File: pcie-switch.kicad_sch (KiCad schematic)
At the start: 82 parts, among them Q2 BSS138PW,115, Q3 BSS138PW,115, U1 PI7C9X3G606GP, U3 MAX3373EEKA+, U6 NVT4858_XQFN

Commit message: [#100765] Update schematic
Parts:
- added C31, C58: C_220n_0402, antmicro-footprints:C_0402_1005Metric, symbol antmicroCapacitors0402:C_220n_0402
- added R44, R45, R46, R49, R50, R68: R_5k1_0402, antmicro-footprints:R_0402_1005Metric, symbol antmicroResistors0402:R_5k1_0402
- added R47, R48, R51: R_330R_0402, antmicro-footprints:R_0402_1005Metric, symbol antmicroResistors0402:R_330R_0402
- added R65, R67: R_0R_0402, antmicro-footprints:R_0402_1005Metric, symbol antmicroResistors0402:R_0R_0402
- added TP1, TP25, TP3, TP31: TP_0.75mm_SMD, antmicro-footprints:TP_SMD_0.75mm, symbol antmicroTestPoints:TP_0.75mm_SMD
- added TP16, TP17: TP_1mm_SMD, antmicro-footprints:TP_SMD_1mm, symbol antmicroTestPoints:TP_1mm_SMD
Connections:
- net +1V8: now also R44.2, R45.2, R46.2, R49.1, R50.1, R68.2
- net C_MODE0: now also R46.1, R48.2
- net C_MODE1: now also R45.1, R47.2
- net GND: now also Q2.2 (S), Q3.2 (S), R47.1, R48.1, R51.2; no longer R21.1, R38.1
- net MISO: no longer U1.M11 (~{EECS})
- net PCIe_{x2_1}.RX0_N: no longer U1.M10 (PER5_N)
- net PCIe_{x2_1}.RX0_P: no longer U1.M9 (PER5_P)
- net PCIe_{x2_1}.TX0_N: no longer C22.2
- net PCIe_{x2_1}.TX0_P: no longer C21.2
- net PCIe_{x2}.~{RST}: now also TP31.1
- net at U1.A1 (REFCLKO1_N): now also TP25.1
- net at U1.A2 (REFCLKO1_P): now also TP3.1
- net at U1.A7 (PER1_N): now also R67.2
- net at U1.A8 (PER1_P): now also R65.2
- net at U1.C7 (PET1_N): now also C58.2
- net at U1.C8 (PET1_P): now also C31.2
- net ~{CLKREQ1}: now reaches U1.E4 (~{CLKREQ1})
- net ~{CLKREQ1}: now also R68.1, TP1.1
- net at R35.1, U1.M1 (SHDA_I2C): now also TP17.1
- net at D1.1 (C): now also R21.2; no longer Q2.3 (D)
- net ~{PM_L11_EN}: now reaches U1.E1 (~{PM_L11_EN})
- net ~{PM_L11_EN}: now also R50.2, R51.1
- net at U1.E9 (~{HOT_PLUG_EN}): now also R49.2
- net at R34.1, U1.L1 (SHCL_I2C): now also TP16.1
- net at U1.M2 (~{SHPCINT}): now also R44.1
- net at D2.1 (C): now also R38.2; no longer Q3.3 (D)
- net JTAG_TCK renamed TCK
- net JTAG_TDI renamed TDI
- net JTAG_TDO renamed TDO
- net JTAG_TMS renamed TMS
- net JTAG_~{RESET} renamed ~{RESET}
- new net: Q2.3 (D), R21.1
- new net: Q3.3 (D), R38.1
- new net CS: U1.M11 (~{EECS})
- new net PCIe_{x2_1}.RX1_N: U1.M10 (PER5_N)
- new net PCIe_{x2_1}.RX1_P: U1.M9 (PER5_P)
- new net PCIe_{x2_1}.TX1_N: C22.2
- new net PCIe_{x2_1}.TX1_P: C21.2
- new net PCIe_{x2}.RX1_N: C58.1
- new net PCIe_{x2}.RX1_P: C31.1
- new net PCIe_{x2}.TX1_N: R67.1
- new net PCIe_{x2}.TX1_P: R65.1
- no-connect marks 27 -> 19
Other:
- note added: "Chip Mode bootstrap"
- note added: "Details: p.28 in the datasheet"
- note added: "HP disabled"
- note added: "Hot Plug LEDs"
- note added: "JTAG"
- note added: "SPI EEPROM & I2C"
- moved on the sheet: C15, C16, C17, C35, C36, C40, C42, C44, C45, C5, C6, D1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

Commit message: [#100765] Change sheet format to A3, update schematic
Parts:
- removed D3, D4, D5: LED_G_0603_LG_L29K-G2J1-24-Z, antmicro-footprints:LED_0603_1608Metric_G, symbol antmicroLEDIndicationDiscrete:LED_G_0603_LG_L29K-G2J1-24-Z
- removed R39, R41: R_470R_0402, antmicro-footprints:R_0402_1005Metric, symbol antmicroResistors0402:R_470R_0402
- removed U6: NVT4858_XQFN, antmicro-footprints:SOT1161-2, symbol antmicroLogicTranslatorsLevelShifters:NVT4858_XQFN
- added D10, D8, D9: LED_G_0603_LG_L29K-G2J1-24-Z, antmicro-footprints:LED_0603_1608Metric_G, symbol antmicroLEDIndicationDiscrete:LED_G_0603_LG_L29K-G2J1-24-Z
- added Q7, Q8, Q9: BSS138PW,115, antmicro-footprints:SC70-3, symbol antmicroTransistorsFETsMOSFETsSingle:BSS138PW,115
- added R18, R82: R_470R_0402, antmicro-footprints:R_0402_1005Metric, symbol antmicroResistors0402:R_470R_0402
- added R19, R39, R41: R_10k_0402, antmicro-footprints:R_0402_1005Metric, symbol antmicroResistors0402:R_10k_0402
- added TP32: TP_1mm_SMD, antmicro-footprints:TP_SMD_1mm, symbol antmicroTestPoints:TP_1mm_SMD
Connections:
- net +1V8: now also R19.2, R39.2, R41.2
- net +3V3: now also Q7.3 (D), Q8.3 (D), Q9.3 (D)
- net GND: now also R40.2, R18.2, R82.2
- net at U1.E10 (~{PORTGOOD1}): now also TP32.1
- net at R40.1: now also D9.1 (C)
- net ~{PGOOD0} renamed ~{PORTGOOD0}
- net ~{PORTGOOD0}: now also Q7.1 (G), R19.1
- net ~{PGOOD4} renamed ~{PORTGOOD4}
- net ~{PORTGOOD4}: now also Q8.1 (G), R39.1
- net ~{PGOOD5} renamed ~{PORTGOOD5}
- net ~{PORTGOOD5}: now also Q9.1 (G), R41.1
- new net: D9.2 (A), Q8.2 (S)
- new net: D10.2 (A), Q9.2 (S)
- new net: D10.1 (C), R82.1
- new net: D8.1 (C), R18.1
- new net: D8.2 (A), Q7.2 (S)
- no-connect marks 19 -> 11
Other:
- note added: "PCIe Switch"
- note added: "Status LEDs"
- company: (none) -> Antmicro
- title: (none) -> antmicro-jetson-orin-baseboard-pcie-switch-expansion-hw
- moved on the sheet: C10, C11, C12, C13, C14, C15, C16, C17, C18, C2, C20, C21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

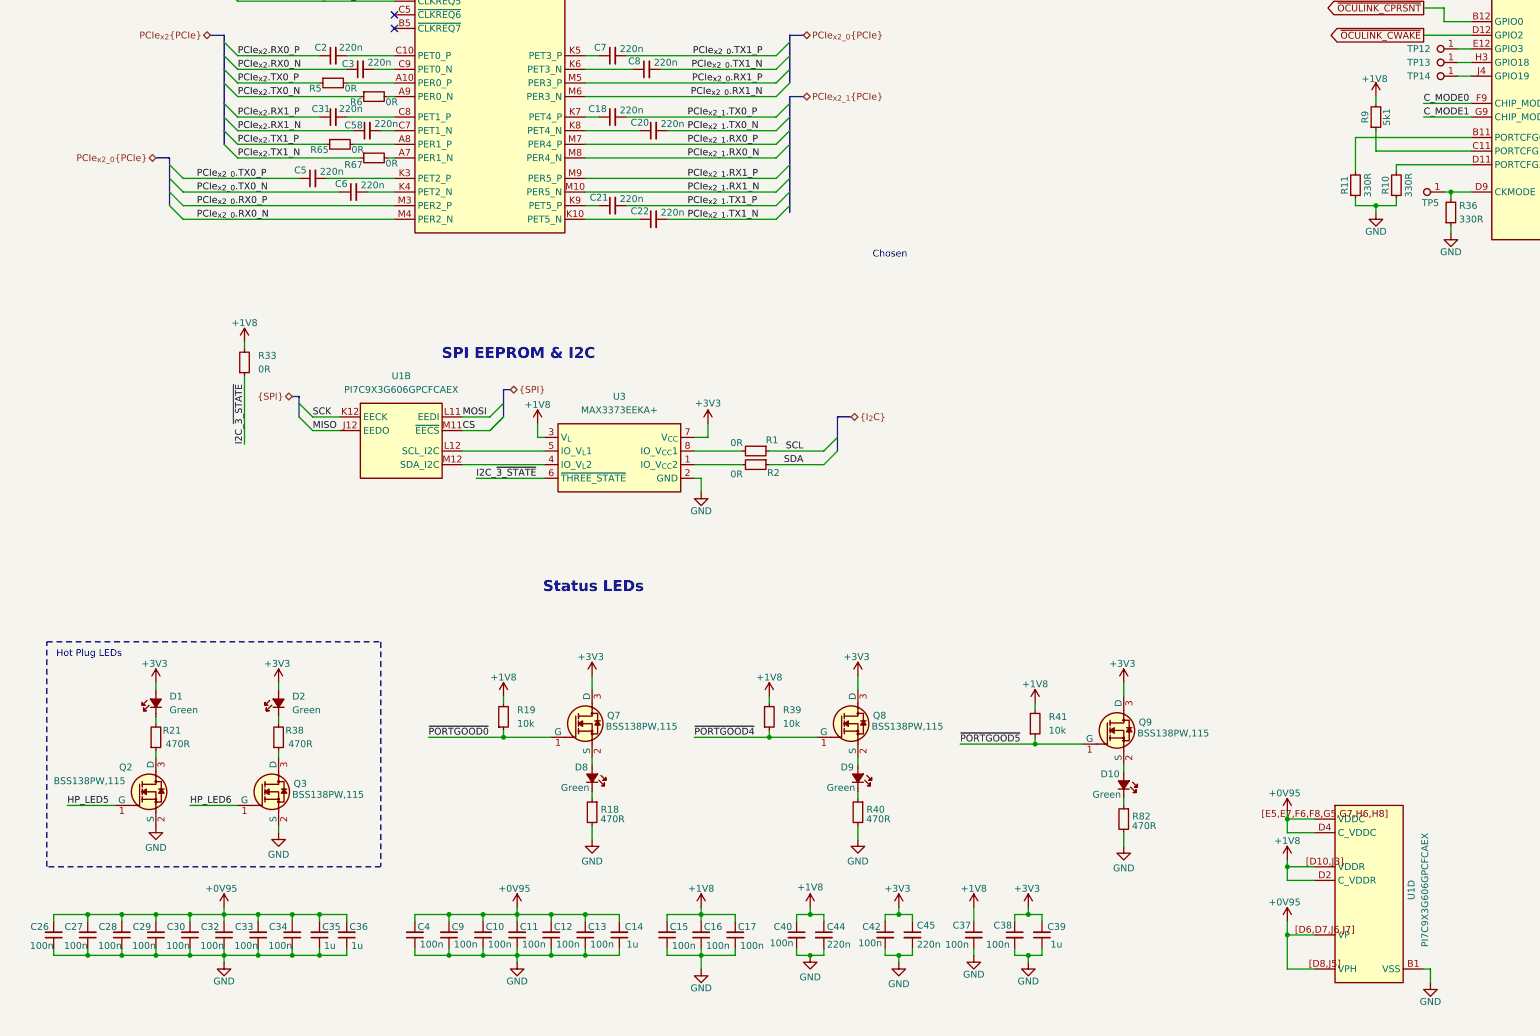
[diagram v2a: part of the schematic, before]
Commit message: [#100765] Prettify decoupling caps
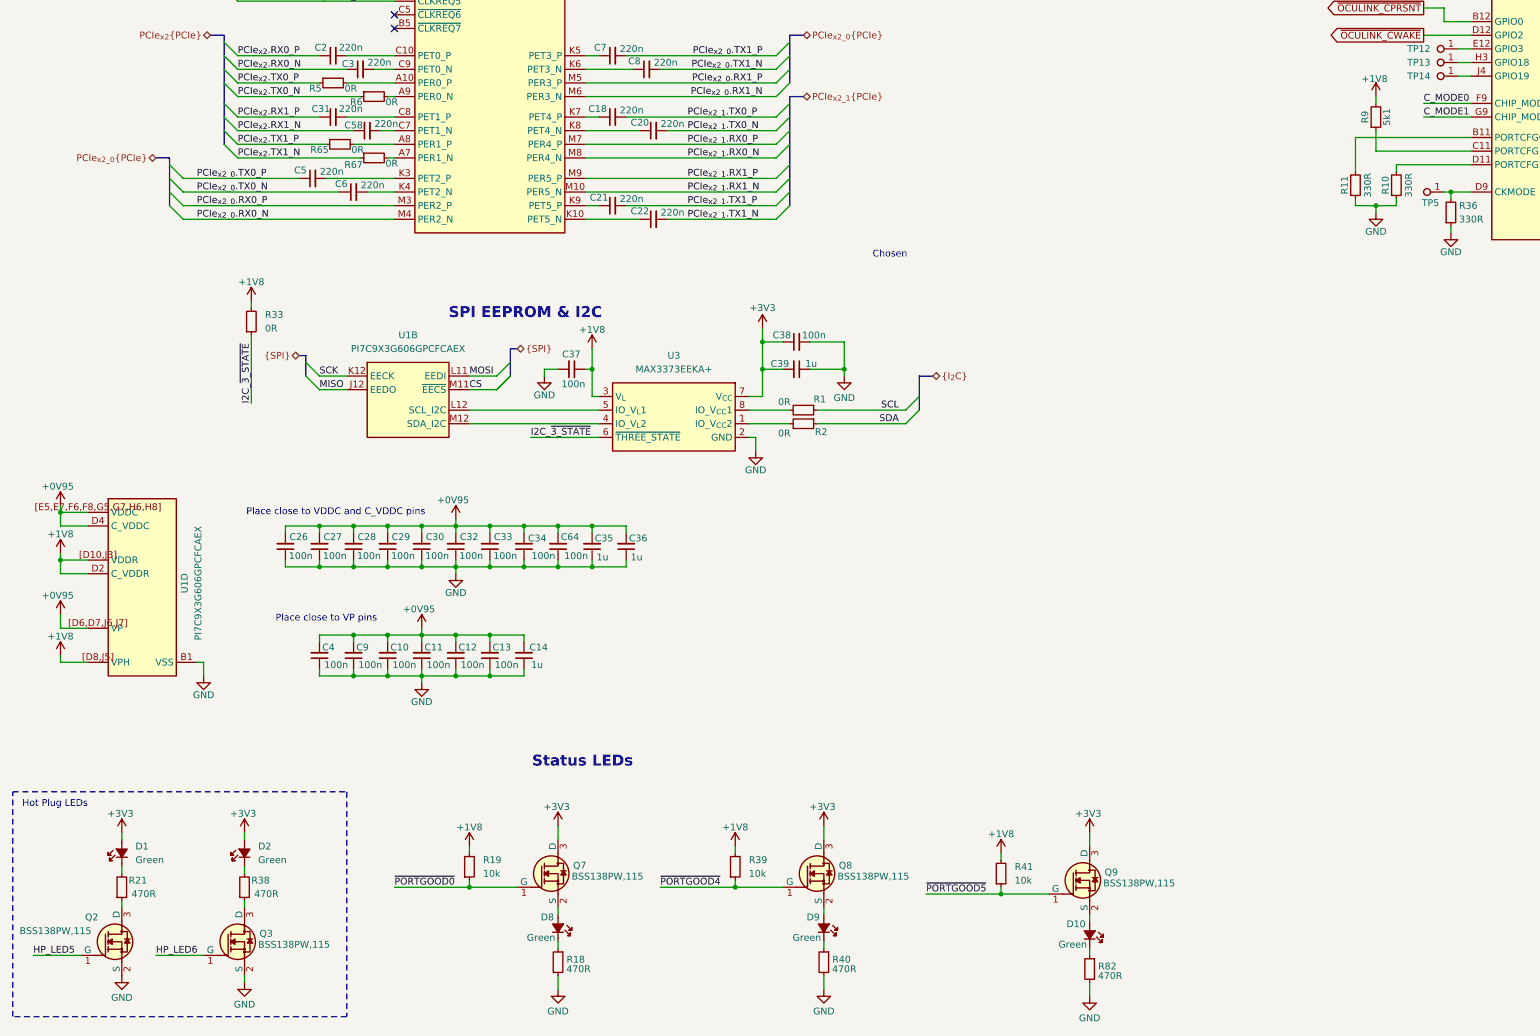
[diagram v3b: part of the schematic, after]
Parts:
- removed C15, C16, C17: C_100n_0402, antmicro-footprints:C_0402_1005Metric, symbol antmicroCapacitors0402:C_100n_0402
- removed C40, C42: C_100n_16V_X7R_0402, antmicro-footprints:C_0402_1005Metric, symbol antmicroCapacitors0402:C_100n_16V_X7R_0402
- removed C44, C45: C_220n_0402, antmicro-footprints:C_0402_1005Metric, symbol antmicroCapacitors0402:C_220n_0402
- added C64: C_100n_0402, antmicro-footprints:C_0402_1005Metric, symbol antmicroCapacitors0402:C_100n_0402
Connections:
- net +0V95: now also C64.2; no longer U1.[D8,J5] (VPH)
- net +1V8: now also U1.[D8,J5] (VPH)
- net GND: now also C64.1
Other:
- note added: "Place close to VDDC and C_VDDC pins"
- note added: "Place close to VP pins"
- moved on the sheet: C10, C11, C12, C13, C14, C26, C27, C28, C29, C30, C32, C33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

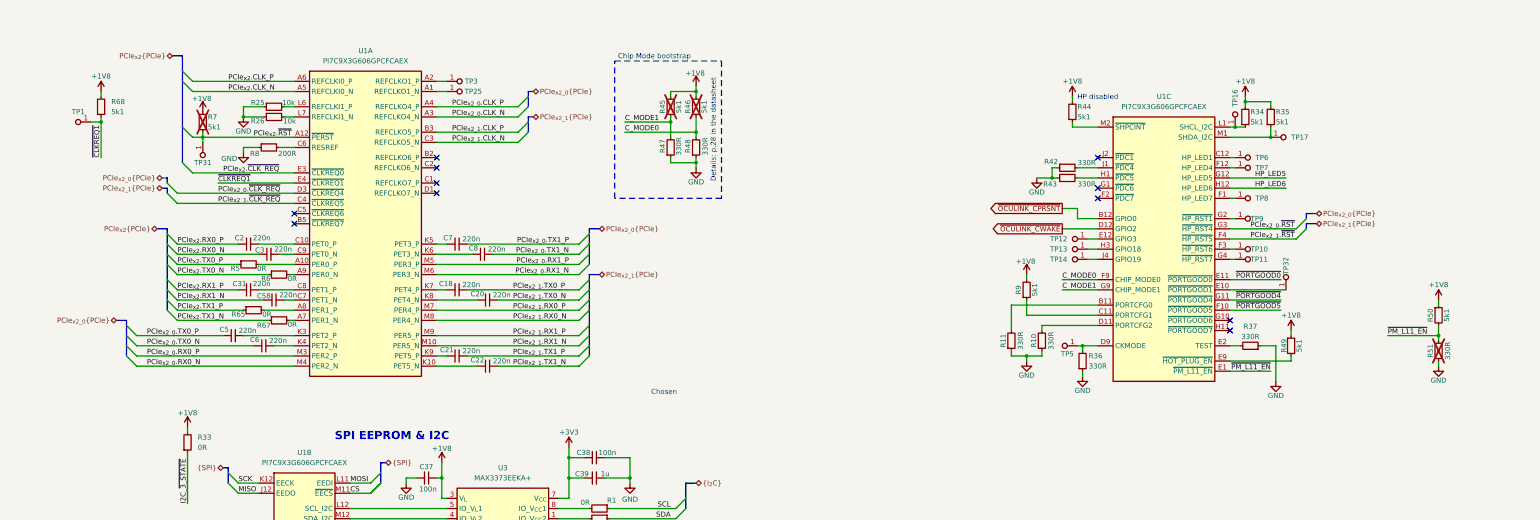
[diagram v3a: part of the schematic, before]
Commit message: [#100765] WIP: Apply review changes
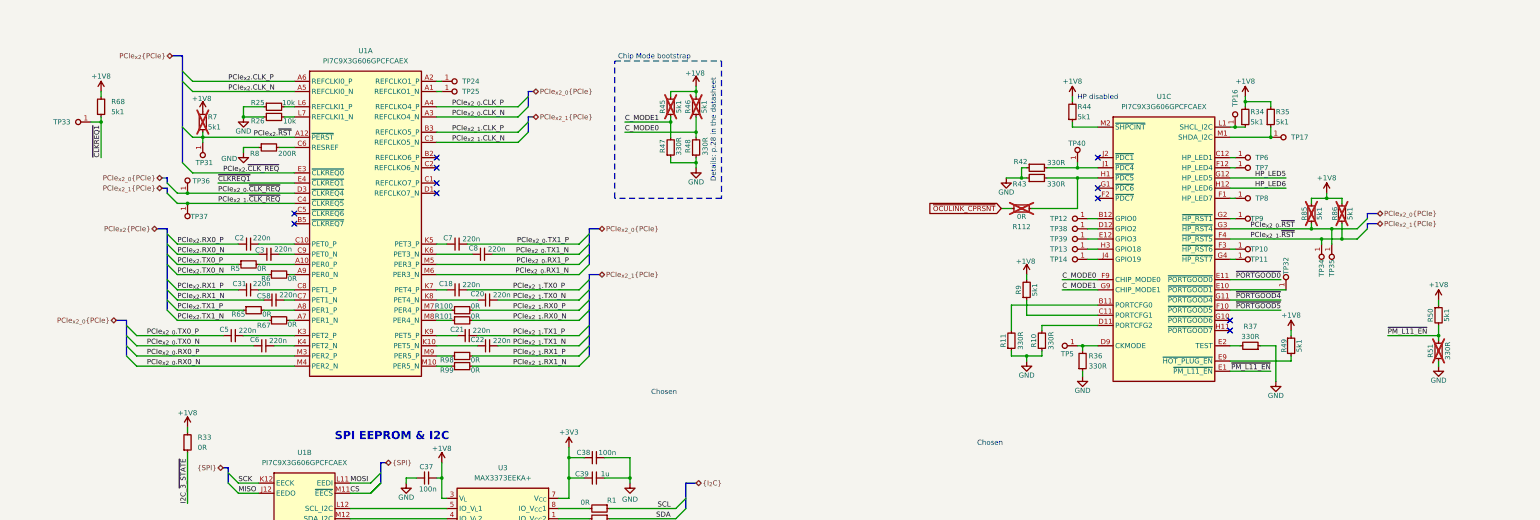
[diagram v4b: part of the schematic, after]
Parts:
- removed TP1, TP25, TP3, TP31: TP_0.75mm_SMD, antmicro-footprints:TP_SMD_0.75mm, symbol antmicroTestPoints:TP_0.75mm_SMD
- added R100, R101, R112, R98, R99: R_0R_0402, antmicro-footprints:R_0402_1005Metric, symbol antmicroResistors0402:R_0R_0402
- added R85, R86: R_5k1_0402, antmicro-footprints:R_0402_1005Metric, symbol antmicroResistors0402:R_5k1_0402
- added TP24, TP25, TP31, TP33, TP34, TP35, TP36, TP37, TP38, TP39, TP40: TP_1mm_SMD, antmicro-footprints:TP_SMD_1mm, symbol antmicroTestPoints:TP_1mm_SMD
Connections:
- net +1V8: now also R85.1, R86.1
- net PCIe_{x2_0}.~{CLK_REQ}: now also TP36.1
- net PCIe_{x2_0}.~{RST}: now also R85.2, TP35.1
- net PCIe_{x2_1}.RX0_N: now also R101.2; no longer U1.M8 (PER4_N)
- net PCIe_{x2_1}.RX0_P: now also R100.2; no longer U1.M7 (PER4_P)
- net PCIe_{x2_1}.RX1_N: now also R99.2; no longer U1.M10 (PER5_N)
- net PCIe_{x2_1}.RX1_P: now also R98.2; no longer U1.M9 (PER5_P)
- net PCIe_{x2_1}.~{CLK_REQ}: now also TP37.1
- net PCIe_{x2_1}.~{RST}: now also R86.2, TP34.1
- net PCIe_{x2}.~{RST}: now also TP31.1
- net ~{CLKREQ1}: now also TP33.1
- net ~{OCULINK_CPRSNT}: now also R112.1; no longer U1.B12 (GPIO0)
- net at U1.A2 (REFCLKO1_P): now also TP24.1
- net at U1.A1 (REFCLKO1_N): now also TP25.1
- net at U1.E12 (GPIO3): now also TP39.1; no longer TP12.1
- net at R43.2, U1.H1 (~{PDC5}): now also R112.2
- net at R42.2, U1.J1 (~{PDC4}): now also TP40.1
- net ~{OCULINK_CWAKE}: no longer names the net of U1.D12 (GPIO2)
- net ~{OCULINK_CWAKE}: now also TP38.1
- new net: R99.1, U1.M10 (PER5_N)
- new net: R100.1, U1.M7 (PER4_P)
- new net: R101.1, U1.M8 (PER4_N)
- new net: R98.1, U1.M9 (PER5_P)
- new net: TP12.1, U1.B12 (GPIO0)
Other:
- moved on the sheet: C21, C22, R42, R43, TP12

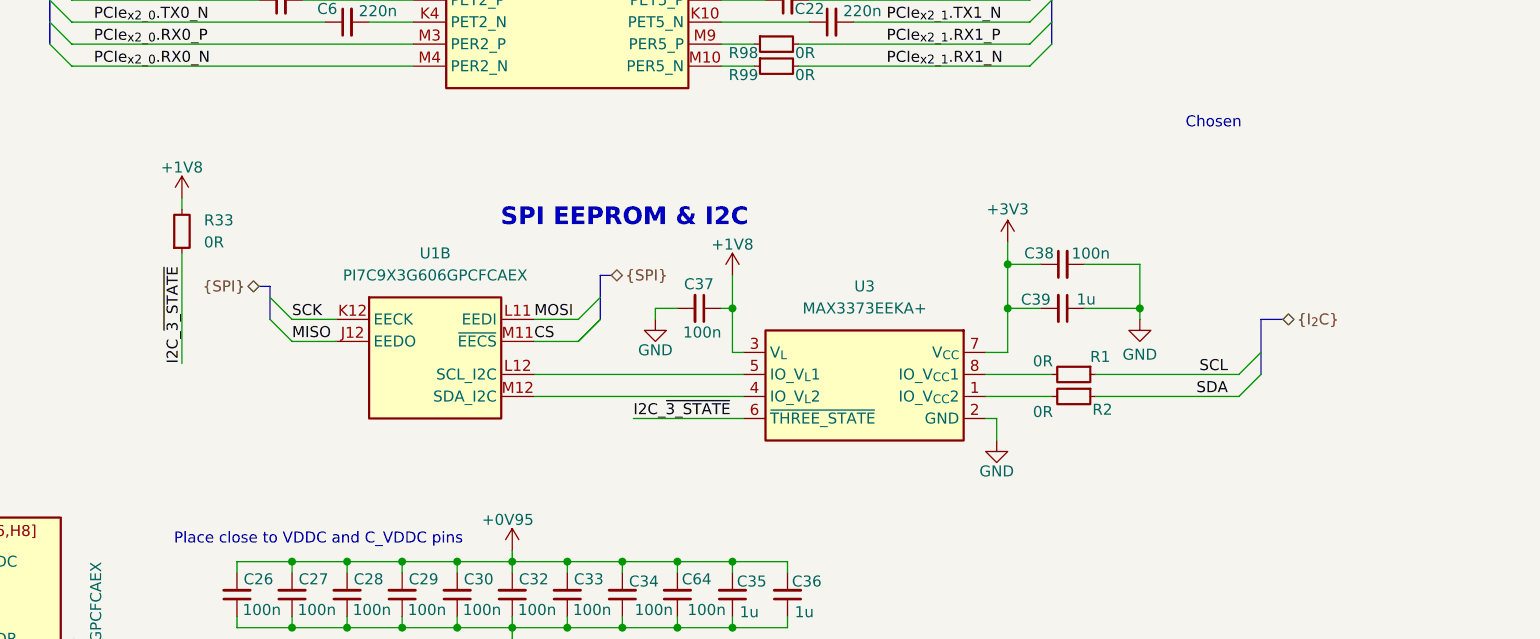
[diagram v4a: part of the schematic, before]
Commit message: [#100765] Change MAX3373EEKA+ to NTS0302JKZ
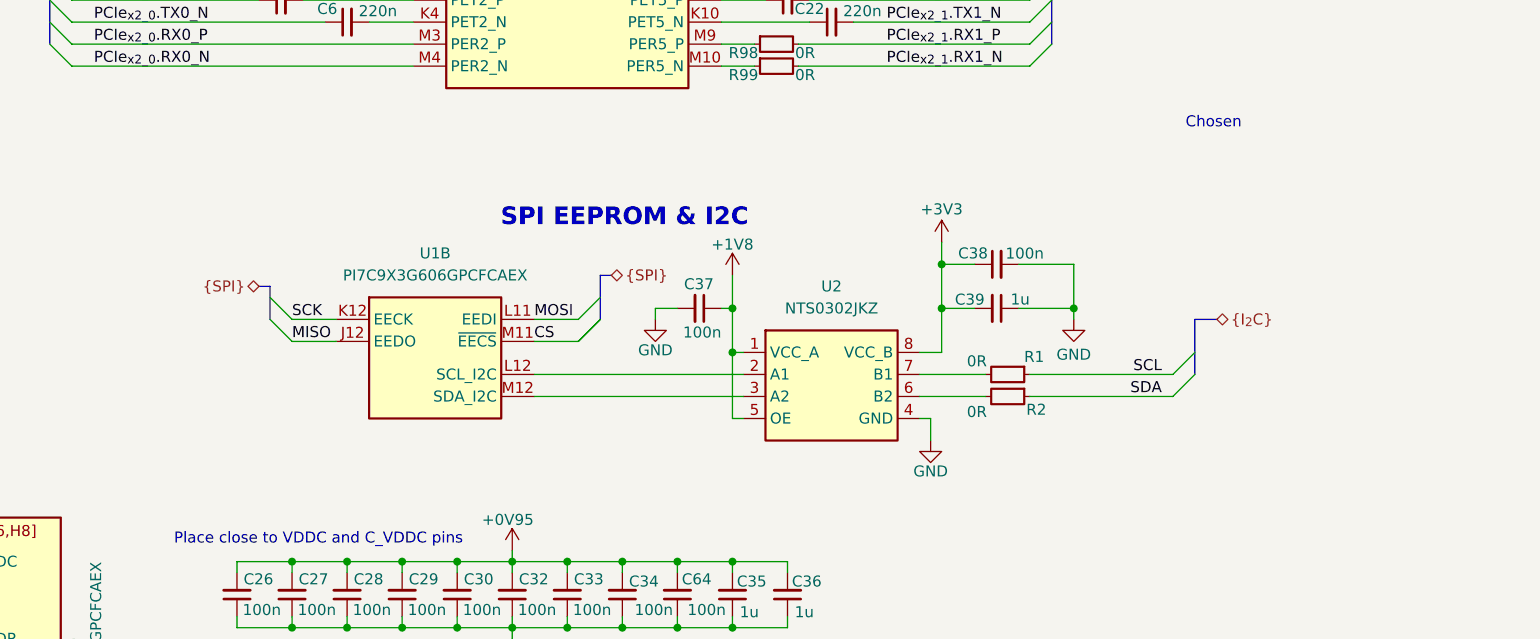
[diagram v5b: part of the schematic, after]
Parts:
- removed R33: R_0R_0402, antmicro-footprints:R_0402_1005Metric, symbol antmicroResistors0402:R_0R_0402
- removed U3: MAX3373EEKA+, antmicro-footprints:SOT-23-8, symbol antmicroLogicTranslatorsLevelShifters:MAX3373EEKA+
- added U2: NTS0302JKZ, antmicro-footprints:X2SON8_1.4x1x0.32mm_P0.35mm, symbol antmicroLogicTranslatorsLevelShifters:NTS0302JKZ
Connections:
- net +1V8: now also U2.1 (VCC_A), U2.5 (OE)
- net +3V3: now also U2.8 (VCC_B)
- net GND: now also U2.4 (GND)
- net at R2.2: now also U2.6 (B2)
- net at U1.M12 (SDA_I2C): now also U2.3 (A2)
- net at U1.L12 (SCL_I2C): now also U2.2 (A1)
- net at R1.2: now also U2.7 (B1)
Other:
- moved on the sheet: C38, C39, R1, R2
